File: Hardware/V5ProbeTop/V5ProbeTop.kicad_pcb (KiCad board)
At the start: 2 copper layers, 126.4 x 15.2 mm, 8 parts

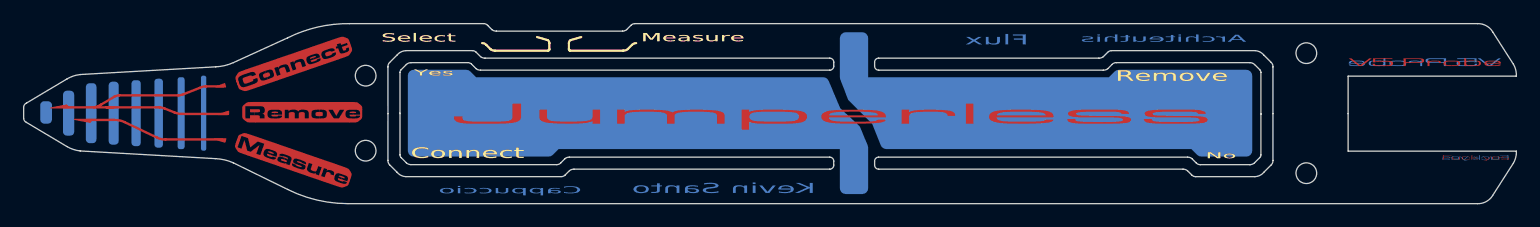
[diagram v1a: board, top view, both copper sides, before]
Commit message: pulled out dome debug prints, fixed fab complaints
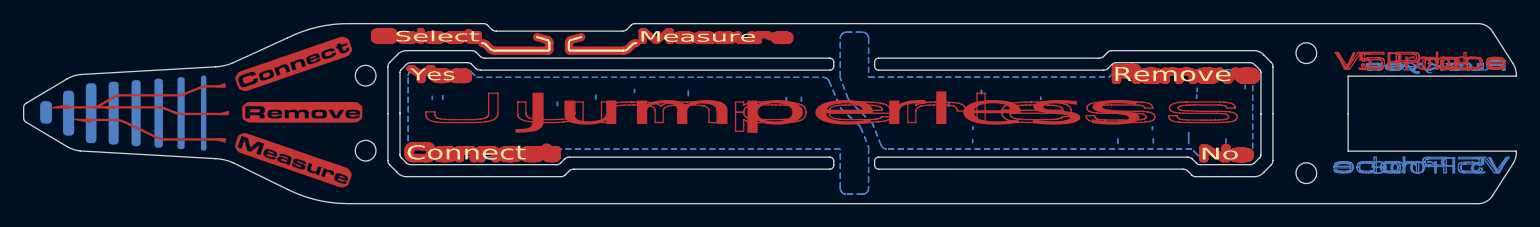
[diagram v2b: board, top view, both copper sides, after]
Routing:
- net (no net): track 0.00 -> 6.98 mm
- added copper zone on B.Cu, net (none)
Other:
- board text added: "Fuck yes"
- board text added: "Jumperless"
- board text added: "V5 Probe"
- board text removed: "Architeuthis"
- board text removed: "Cappuccio"
- board text removed: "Flux"
- board text removed: "Kevin Santo"

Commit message: routed V5r4
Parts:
- added J1: Conn_01x13_Socket, JumperlessFootprints:Probe_capsense_connect, B.Cu at (159.7, 92.4)
- added J2: Conn_01x13_Socket, JumperlessFootprints:Probe_capsense_connect, B.Cu at (159.7, 80.1)
- added TP1: TestPoint, JumperlessFootprints:Tiniest_Possible_pad, B.Cu at (114.2, 89.4)
- added TP10: TestPoint, JumperlessFootprints:Tiniest_Possible_pad, B.Cu at (152.6, 88.9)
- added TP11: TestPoint, JumperlessFootprints:Tiniest_Possible_pad, B.Cu at (157.8, 83.3)
- added TP12: TestPoint, JumperlessFootprints:Tiniest_Possible_pad, B.Cu at (162.8, 88.9)
- added TP13: TestPoint, JumperlessFootprints:Tiniest_Possible_pad, B.Cu at (167.9, 88.9)
- added TP14: TestPoint, JumperlessFootprints:Tiniest_Possible_pad, B.Cu at (87.9, 89.0)
- added TP15: TestPoint, JumperlessFootprints:Tiniest_Possible_pad, B.Cu at (113.7, 83.3)
- added TP16: TestPoint, JumperlessFootprints:Tiniest_Possible_pad, B.Cu at (118.8, 83.3)
- added TP17: TestPoint, JumperlessFootprints:Tiniest_Possible_pad, B.Cu at (124.2, 83.3)
- added TP18: TestPoint, JumperlessFootprints:Tiniest_Possible_pad, B.Cu at (129.4, 83.3)
- added TP19: TestPoint, JumperlessFootprints:Tiniest_Possible_pad, B.Cu at (134.5, 83.3)
- added TP2: TestPoint, JumperlessFootprints:Tiniest_Possible_pad, B.Cu at (118.8, 88.9)
- added TP20: TestPoint, JumperlessFootprints:Tiniest_Possible_pad, B.Cu at (139.7, 83.3)
- added TP21: TestPoint, JumperlessFootprints:Tiniest_Possible_pad, B.Cu at (144.3, 83.3)
- added TP22: TestPoint, JumperlessFootprints:Tiniest_Possible_pad, B.Cu at (145.4, 83.6)
- added TP23: TestPoint, JumperlessFootprints:Tiniest_Possible_pad, B.Cu at (147.2, 83.3)
- added TP24: TestPoint, JumperlessFootprints:Tiniest_Possible_pad, B.Cu at (152.6, 83.3)
- added TP25: TestPoint, JumperlessFootprints:Tiniest_Possible_pad, B.Cu at (157.8, 88.9)
- added TP26: TestPoint, JumperlessFootprints:Tiniest_Possible_pad, B.Cu at (162.8, 83.3)
- added TP27: TestPoint, JumperlessFootprints:Tiniest_Possible_pad, B.Cu at (167.8, 82.8)
- added TP28: TestPoint, JumperlessFootprints:Tiniest_Possible_pad, B.Cu at (87.9, 83.1)
- added TP3: TestPoint, JumperlessFootprints:Tiniest_Possible_pad, B.Cu at (124.2, 88.9)
- added TP4: TestPoint, JumperlessFootprints:Tiniest_Possible_pad, B.Cu at (129.4, 88.9)
- added TP5: TestPoint, JumperlessFootprints:Tiniest_Possible_pad, B.Cu at (134.5, 88.9)
- added TP6: TestPoint, JumperlessFootprints:Tiniest_Possible_pad, B.Cu at (139.7, 88.9)
- added TP7: TestPoint, JumperlessFootprints:Tiniest_Possible_pad, B.Cu at (144.3, 89.0)
- added TP8: TestPoint, JumperlessFootprints:Tiniest_Possible_pad, B.Cu at (145.4, 88.8)
- added TP9: TestPoint, JumperlessFootprints:Tiniest_Possible_pad, B.Cu at (147.2, 88.9)
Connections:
- REF** pad 1: (no net) -> Net-(J1-Pin_1)
- REF** pad 2: (no net) -> Net-(J1-Pin_1)
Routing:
- net Net-(J1-Pin_2): track 0.00 -> 106.8 mm
- net Net-(J1-Pin_4): track 0.00 -> 101.5 mm
- net Net-(J1-Pin_1): track 0.00 -> 97.6 mm
- net Net-(J1-Pin_3): track 0.00 -> 88.6 mm
- net Net-(J1-Pin_14): track 0.00 -> 65.9 mm
- net Net-(J1-Pin_13): track 0.00 -> 56.7 mm
- net Net-(J1-Pin_12): track 0.00 -> 49.4 mm
- net Net-(J1-Pin_11): track 0.00 -> 40.3 mm
- net Net-(J1-Pin_5): track 0.00 -> 33.5 mm
- net Net-(J1-Pin_10): track 0.00 -> 32.1 mm
- net Net-(J1-Pin_6): track 0.00 -> 31.0 mm
- net Net-(J1-Pin_9): track 0.00 -> 25.1 mm
- net Net-(J1-Pin_8): track 0.00 -> 19.2 mm
- net Net-(J1-Pin_7): track 0.00 -> 13.9 mm
- net (no net): track 6.98 -> 0.00 mm
- added copper zone on B.Cu, net Net-(J1-Pin_10)
- added copper zone on B.Cu, net Net-(J1-Pin_11)
- added copper zone on B.Cu, net Net-(J1-Pin_12)
- added copper zone on B.Cu, net Net-(J1-Pin_13)
- added copper zone on B.Cu, net Net-(J1-Pin_14)
- added copper zone on B.Cu, net Net-(J1-Pin_2)
- added copper zone on B.Cu, net Net-(J1-Pin_3)
- added copper zone on B.Cu, net Net-(J1-Pin_4)
- added copper zone on B.Cu, net Net-(J1-Pin_5)
- added copper zone on B.Cu, net Net-(J1-Pin_6)
- added copper zone on B.Cu, net Net-(J1-Pin_7)
- added copper zone on B.Cu, net Net-(J1-Pin_8)
- added copper zone on B.Cu, net Net-(J1-Pin_9)
- removed copper zone on B.Cu, net (none)
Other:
- outline, holes or cut-outs redrawn

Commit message: Rev 4 hardware
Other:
- board text added: "PCB3D_BR_PROBETOP"
- board text added: "PCB3D_TL_PROBETOP"

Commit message: Add post campaign update draft
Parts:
- moved TP7 0.26 mm to (144.1, 88.9)
- moved TP21 0.26 mm to (144.1, 83.5)
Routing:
- net Net-(J1-Pin_3): track 88.6 -> 90.3 mm
- net Net-(J1-Pin_12): track 49.4 -> 50.3 mm
- net Net-(J1-Pin_6): track 31.0 -> 31.8 mm
- net Net-(J1-Pin_9): track 25.1 -> 25.9 mm
- net Net-(J1-Pin_11): track 40.3 -> 40.9 mm
- net Net-(J1-Pin_14): track 65.9 -> 66.5 mm
- net Net-(J1-Pin_13): track 56.7 -> 57.3 mm
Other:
- outline, holes or cut-outs redrawn
